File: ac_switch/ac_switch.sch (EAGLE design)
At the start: 21 parts, among them IC1 TINY85, IC2 ACS714, T1 BC337

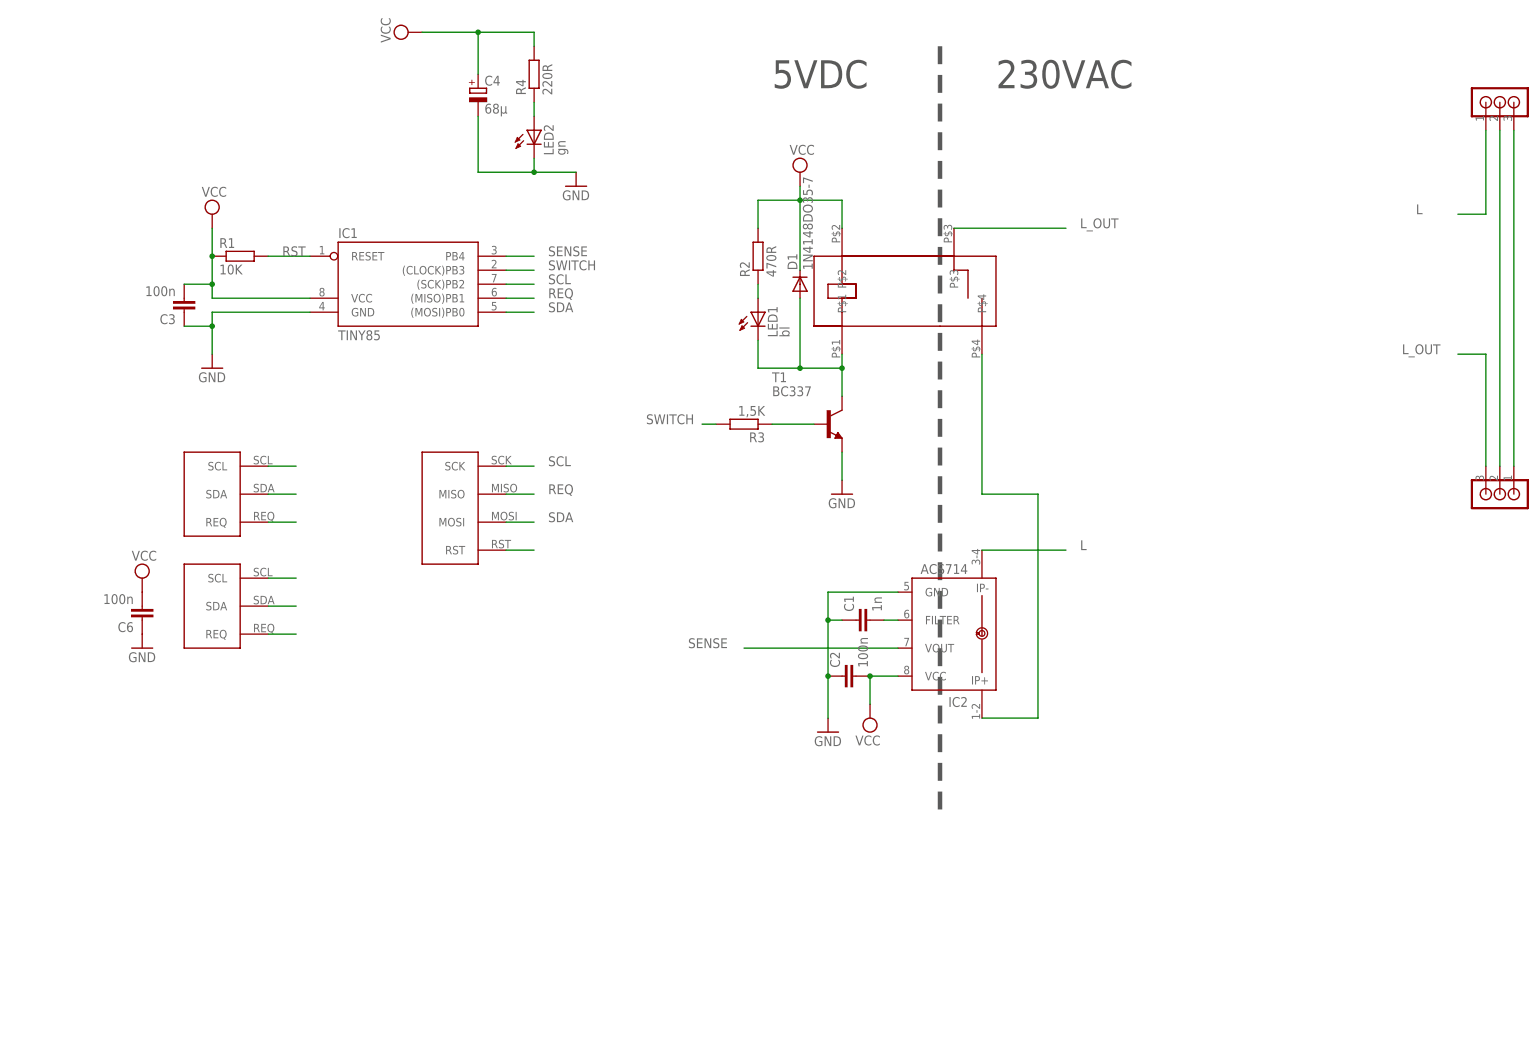
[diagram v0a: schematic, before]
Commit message: Added a fuse and an OP amp to increase signal bandwith.
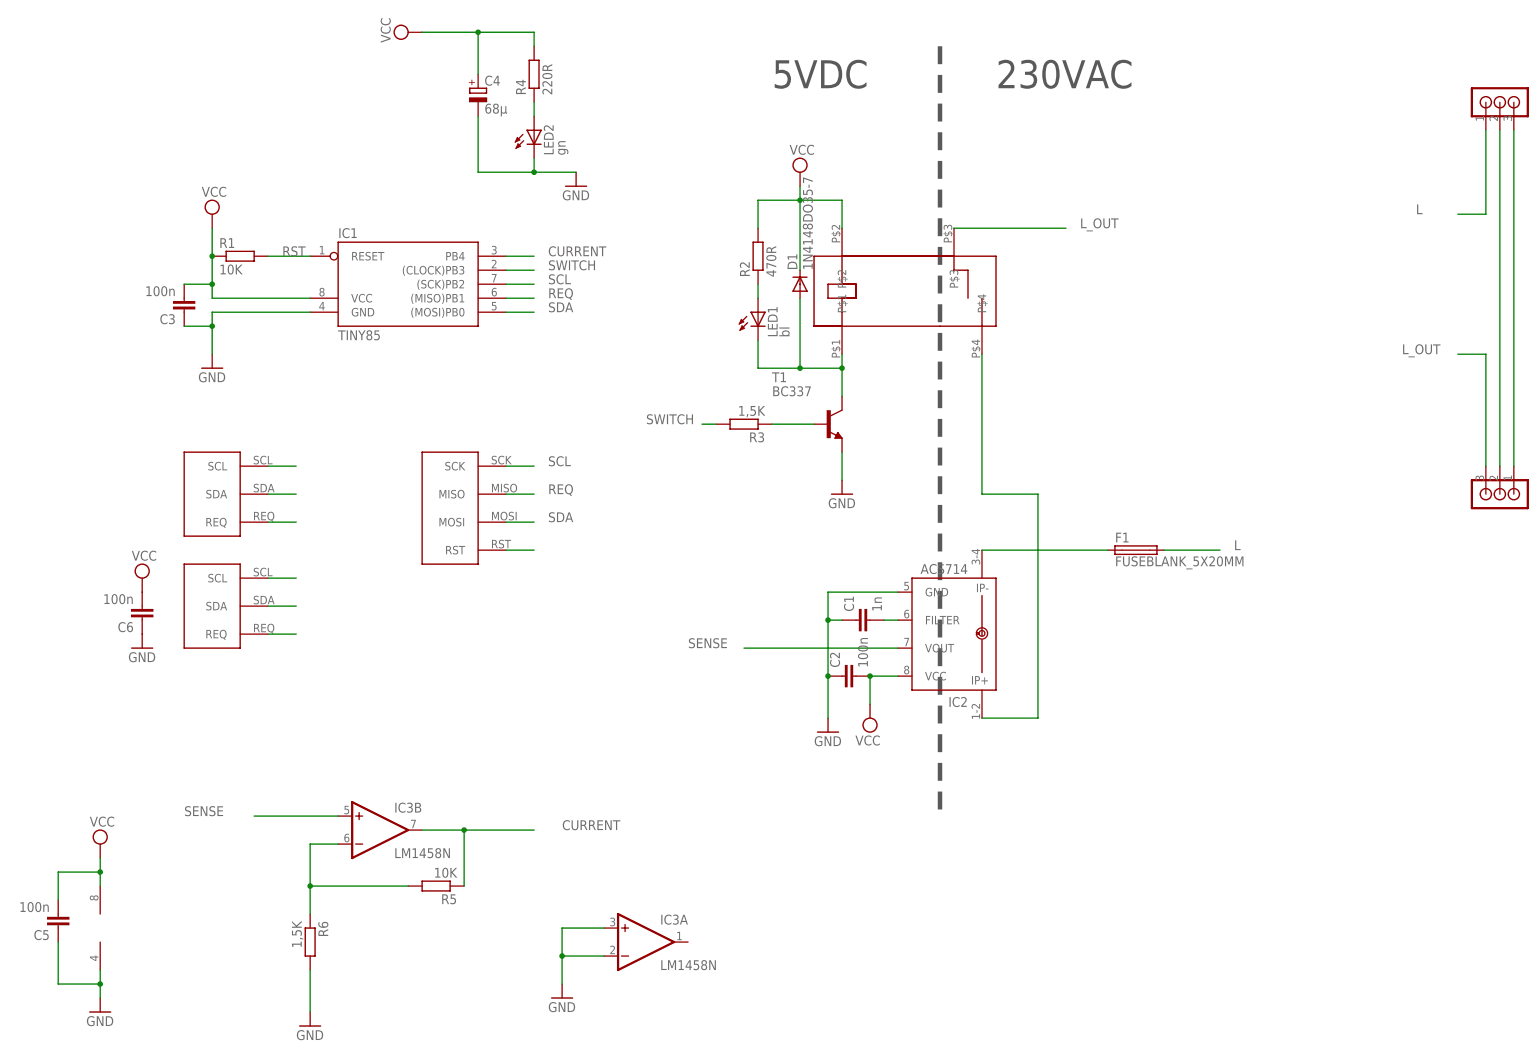
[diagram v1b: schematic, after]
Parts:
- added C5: 100n, resistor:C-EU025-024X044
- added F1: FUSEBLANK_5X20MM, fuse:FUSEBLANK_5X20MM
- added IC3: LM1458N, linear:LM1458N
- added R5: 10K, resistor:R-EU_0207/10
- added R6: 1,5K, resistor:R-EU_0207/10
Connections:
- new net CURRENT: IC1.PB4, IC3B.OUT, R5.1
- new net N$10: IC3B.-IN, R5.2, R6.1
- new net N$7: F1.1, IC2.IP-
- net GND: now also C5.1, IC3A.+IN, IC3A.-IN, IC3P.V-, R6.2
- net L: now also F1.2; no longer IC2.IP-
- net SENSE: now also IC3B.+IN; no longer IC1.PB4
- net VCC: now also C5.2, IC3P.V+
